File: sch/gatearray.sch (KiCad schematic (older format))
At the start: 71 parts, among them X2 CONN-7S

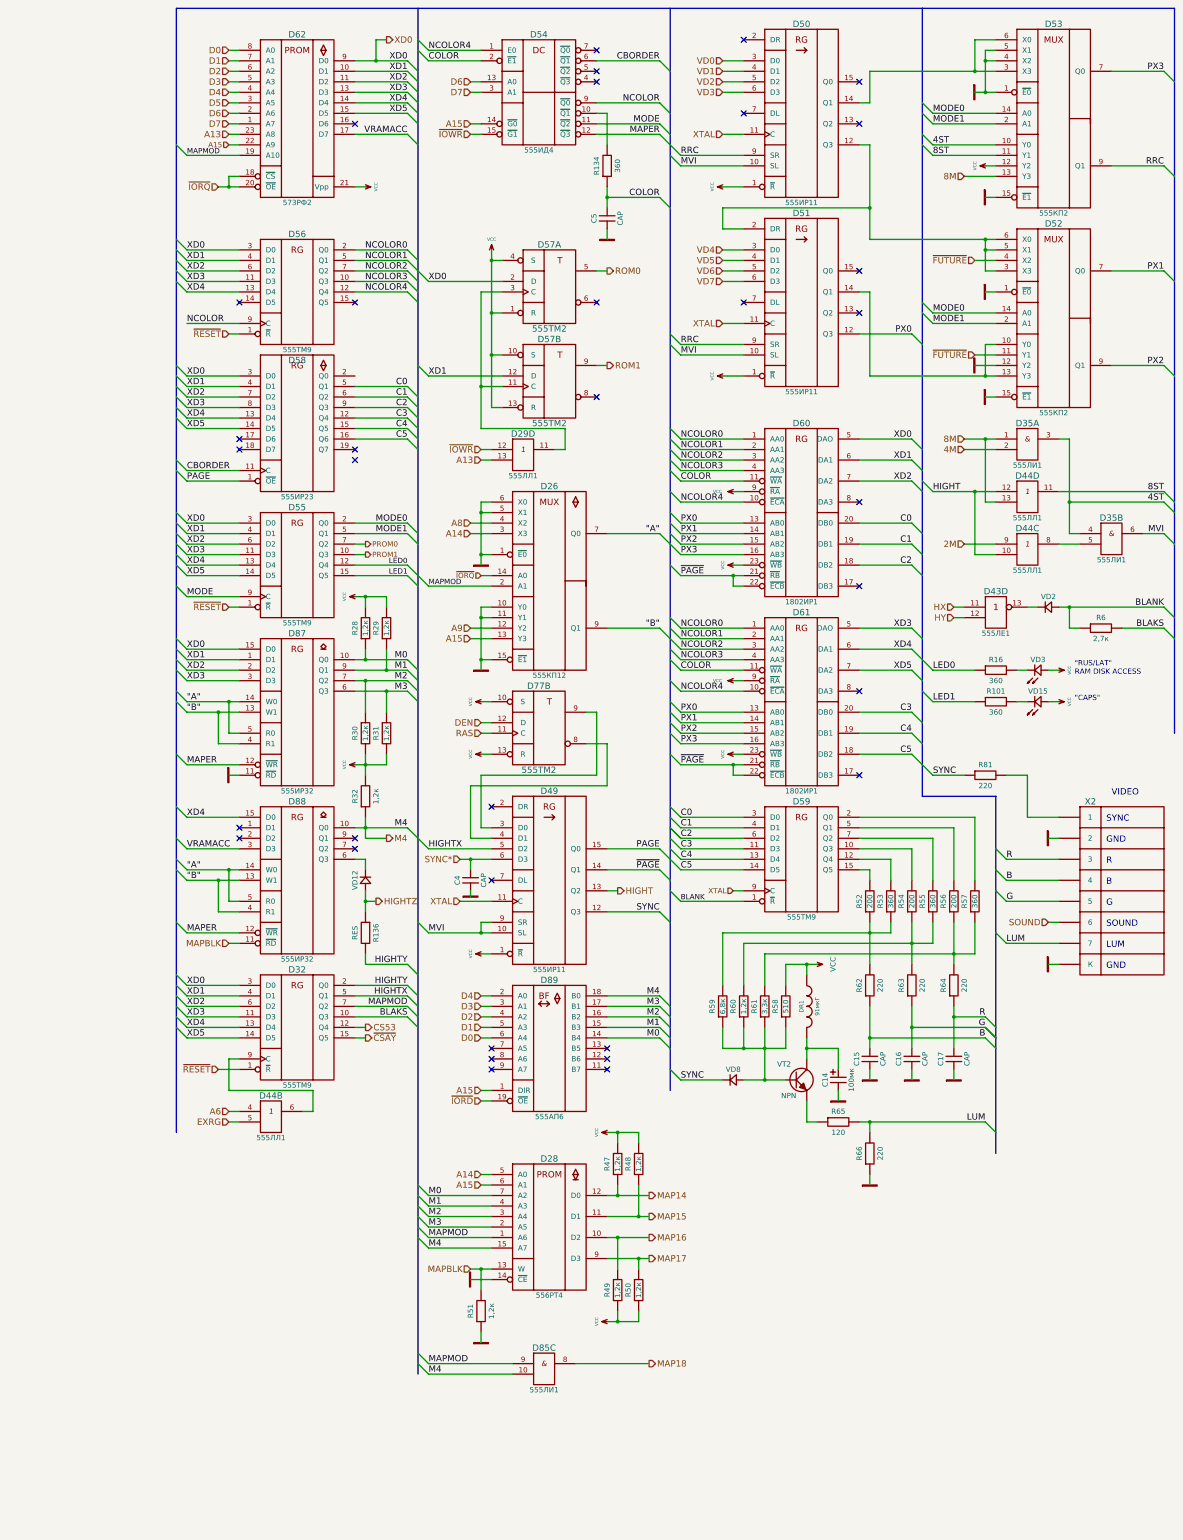
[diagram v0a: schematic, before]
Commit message: Start to move to a bit more affordable components
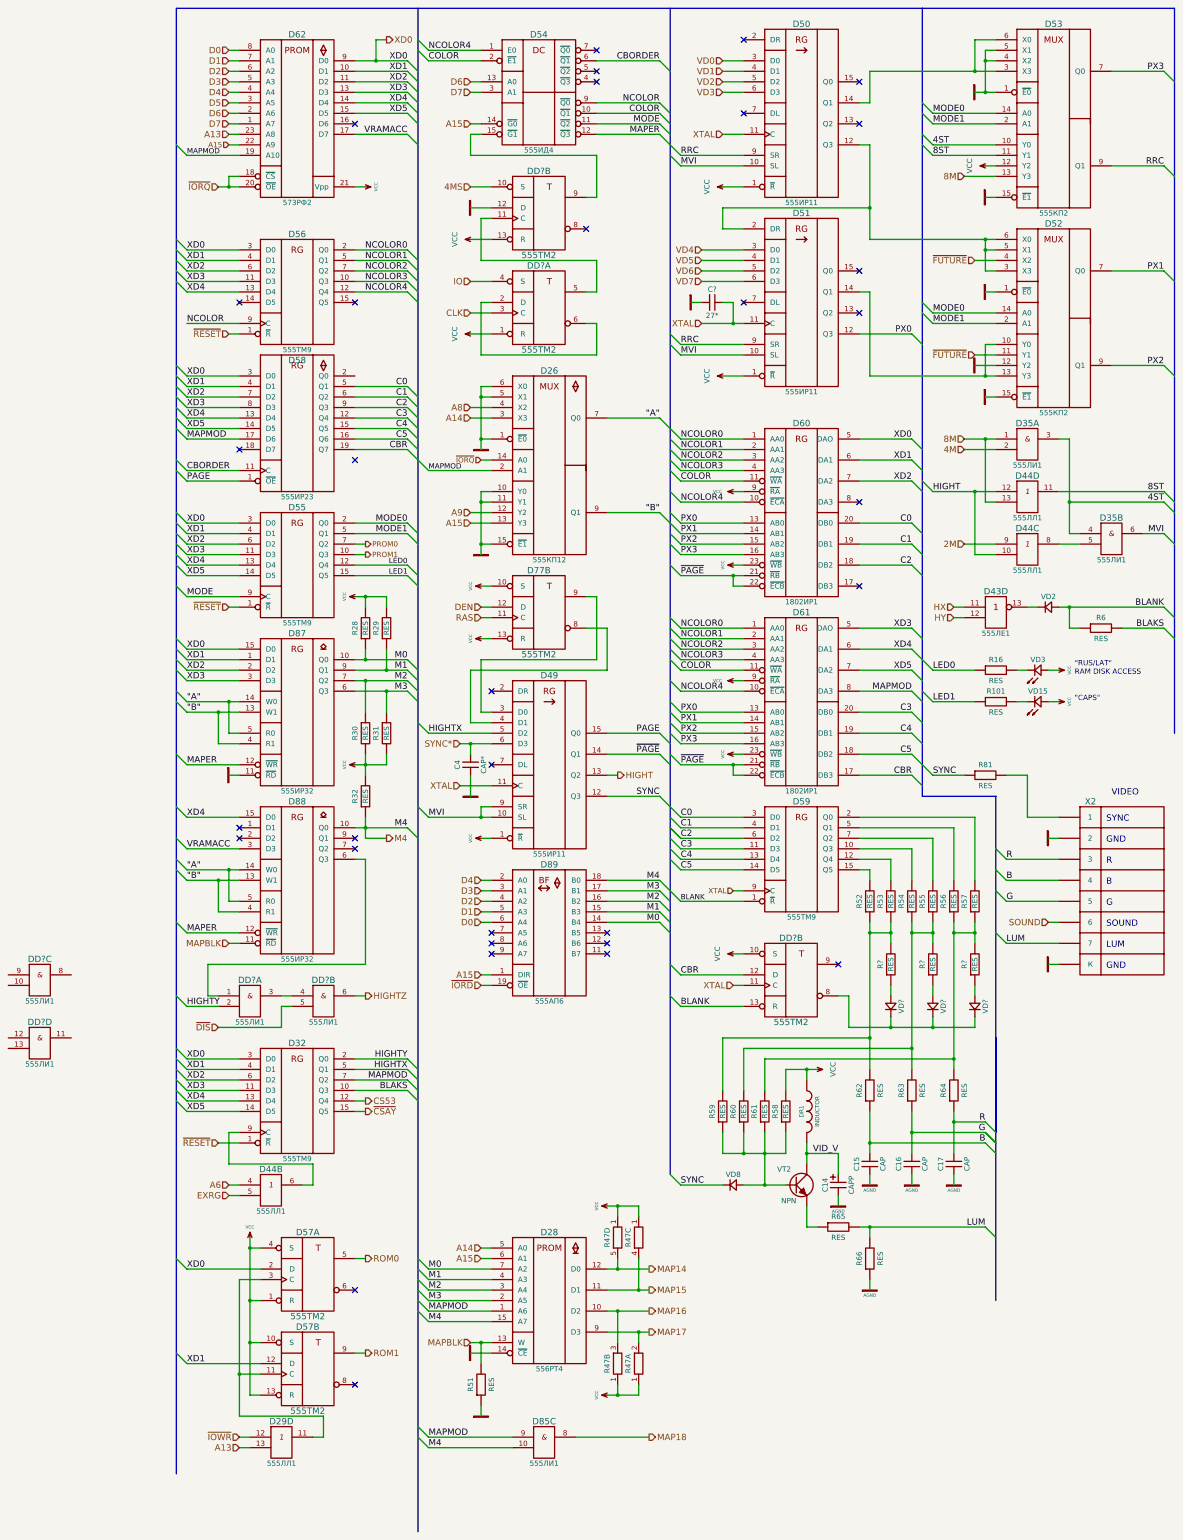
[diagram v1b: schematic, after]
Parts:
- removed C5: CAP, MyLib:C_Disc_D7.5_P2.5, symbol CAP
- removed R134: 360, MyLib:Resistor_Horizontal_RM7.5mm, symbol RES
- removed R136: RES, MyLib:Resistor_Horizontal_RM7.5mm, symbol RES
- removed R47, R48, R49, R50: 1,2к, MyLib:Resistor_Vertical_RM2.5mm, symbol RES
- removed VD12: DIODE_MY, MyLib:Diode_DO-35_SOD27_Horizontal_RM7.5, symbol DIODE_MY
- added C?: 27*, symbol CAP
- added DD? (x4): 555ЛИ1, symbol 555ЛИ1
- added DD? (x3): 555ТМ2, symbol 555ТМ2
- added R47: RES_PACK4_C, MyLib:Resistor_Array_SIP4, symbol RES_PACK4_C
- added R? (x3): RES, MyLib:Resistor_Horizontal_RM7.5mm, symbol RES
- added VD? (x3): DIODE, symbol DIODE
- C14: value 100мк -> CAPP
- C4: value CAP -> CAP*
- DR1: value 91мкГ -> INDUCTOR
- R101, R16, R53, R55, R57: value 360 -> RES
- R28, R29, R30, R31, R32, R51, R60: value 1,2к -> RES
- R52, R54, R56: value 200 -> RES
- R58: value 510 -> RES
- R59: value 6,8к -> RES
- R6: value 2,7к -> RES
- R61: value 3,3к -> RES
- R62, R63, R64, R66, R81: value 220 -> RES
- R65: value 120 -> RES
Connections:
- net BLANK: now also DD?.13 (R)
- net COLOR: now also D54.10 (~Q1)
- net GND: now also C?.1, DD?.12 (D), DD?.7 (GND), DD?.7 (GND), DD?.7 (GND), DD?.7 (GND), DD?.7 (GND), DD?.7 (GND), DD?.7 (GND)
- net HIGHTY: now also DD?.2 (in2)
- net HIGHTZ: now also DD?.6 (out)
- net MAP14: now also R47.5
- net MAP15: now also R47.4
- net MAP16: now also R47.3
- net MAP17: now also R47.2
- net MAPMOD: now also D58.17 (D6), D61.8 (DA3)
- net VCC: now also DD?.1 (R), DD?.10 (S), DD?.13 (R), DD?.14 (VCC), DD?.14 (VCC), DD?.14 (VCC), DD?.14 (VCC), DD?.14 (VCC), DD?.14 (VCC), DD?.14 (VCC), R47.1, R47.1, R47.1, R47.1
- net XTAL: now also C?.2, DD?.11 (C)
- net ~IOWR: no longer D54.15 (~G1)
- net VID_V: now reaches C14.1, DR1.2, VT2.C
- net CBR: now reaches D58.19 (Q7)
- net CBR: now also D61.17 (DB3), DD?.12 (D)
- net at D88.6 (Q3): now also DD?.1 (in1)
- net at R52.1, R53.1, R59.2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: now also R?.2
- net at R54.1, R55.1, R60.2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: now also R?.2
- net at R56.1, R57.1, R61.2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: now also R?.2
- new net: D54.15 (~G1), DD?.9
- new net: DD?.3 (out), DD?.4 (in1)
- new net: DD?.2 (D), DD?.6
- new net: DD?.11 (C), DD?.5
- new net: DD?.8, VD?.1, VD?.1, VD?.1
- new net: R?.1, VD?.2 (x3)
- new net 4MS: DD?.10 (S)
- new net CLK: DD?.3 (C)
- new net IO: DD?.4 (S)
- new net ~DIS: DD?.5 (in2)
- no-connect marks 35 -> 33
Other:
- moved on the sheet: C14, C15, C16, C17, C4, D26, D28, D29D, D32, D44B, D49, D57A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

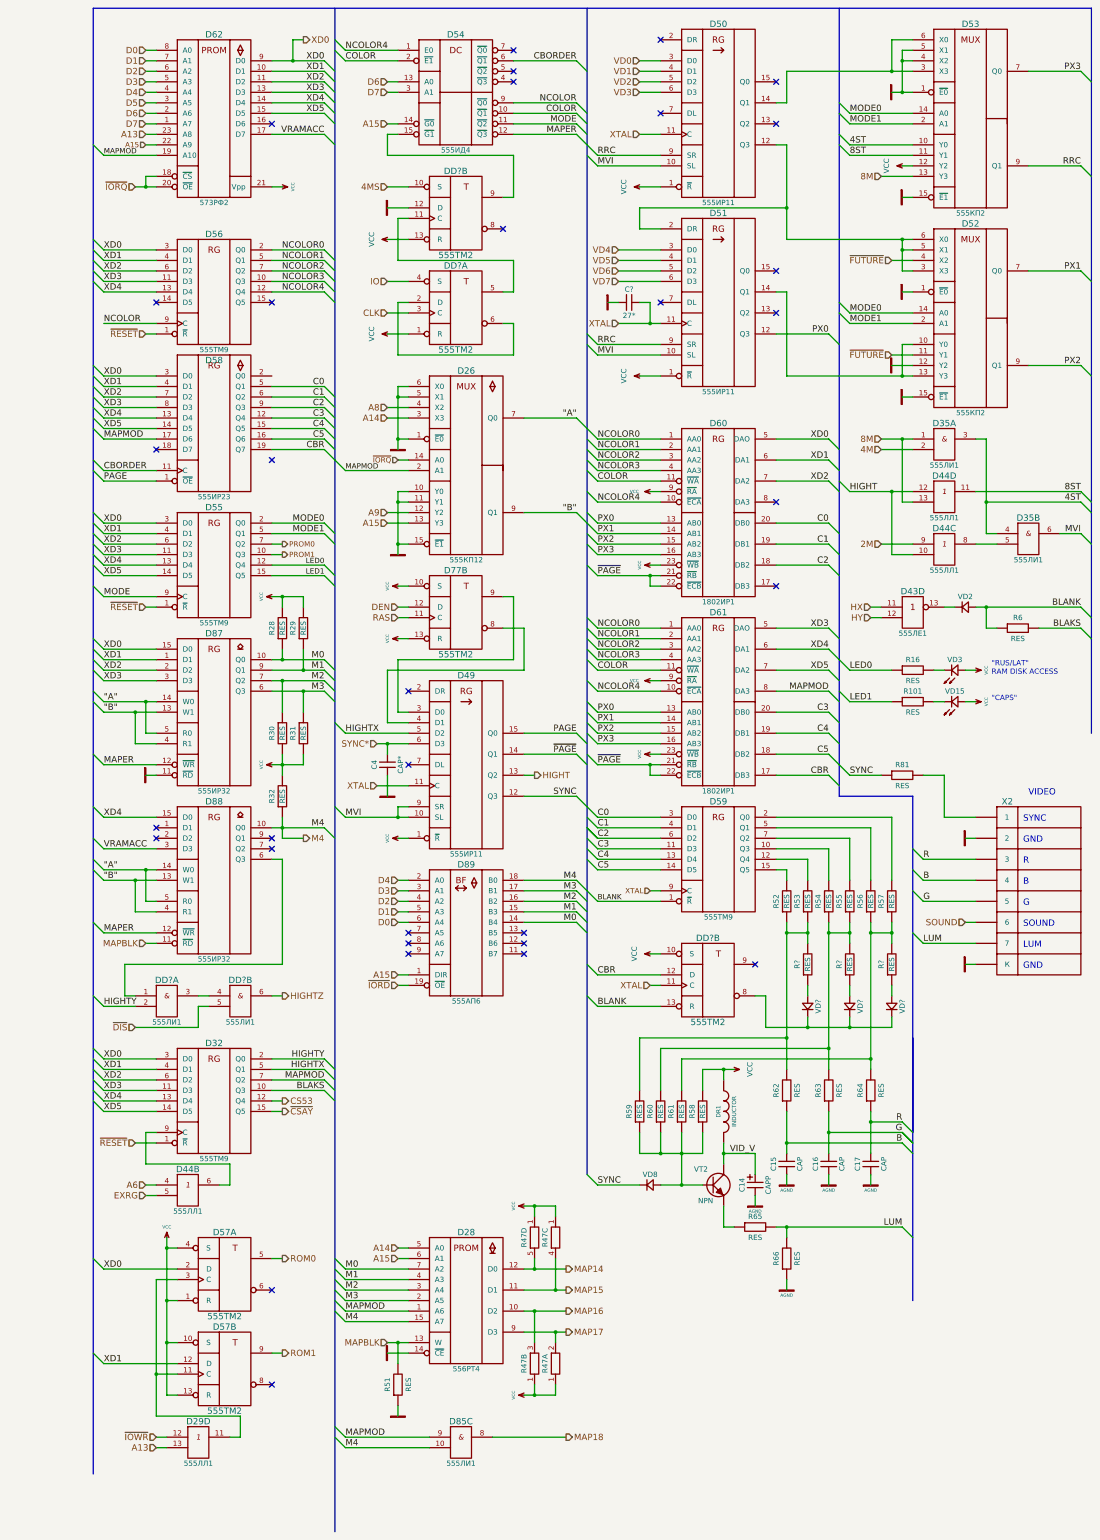
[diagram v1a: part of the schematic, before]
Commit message: Update IR22 and IR23 symbols
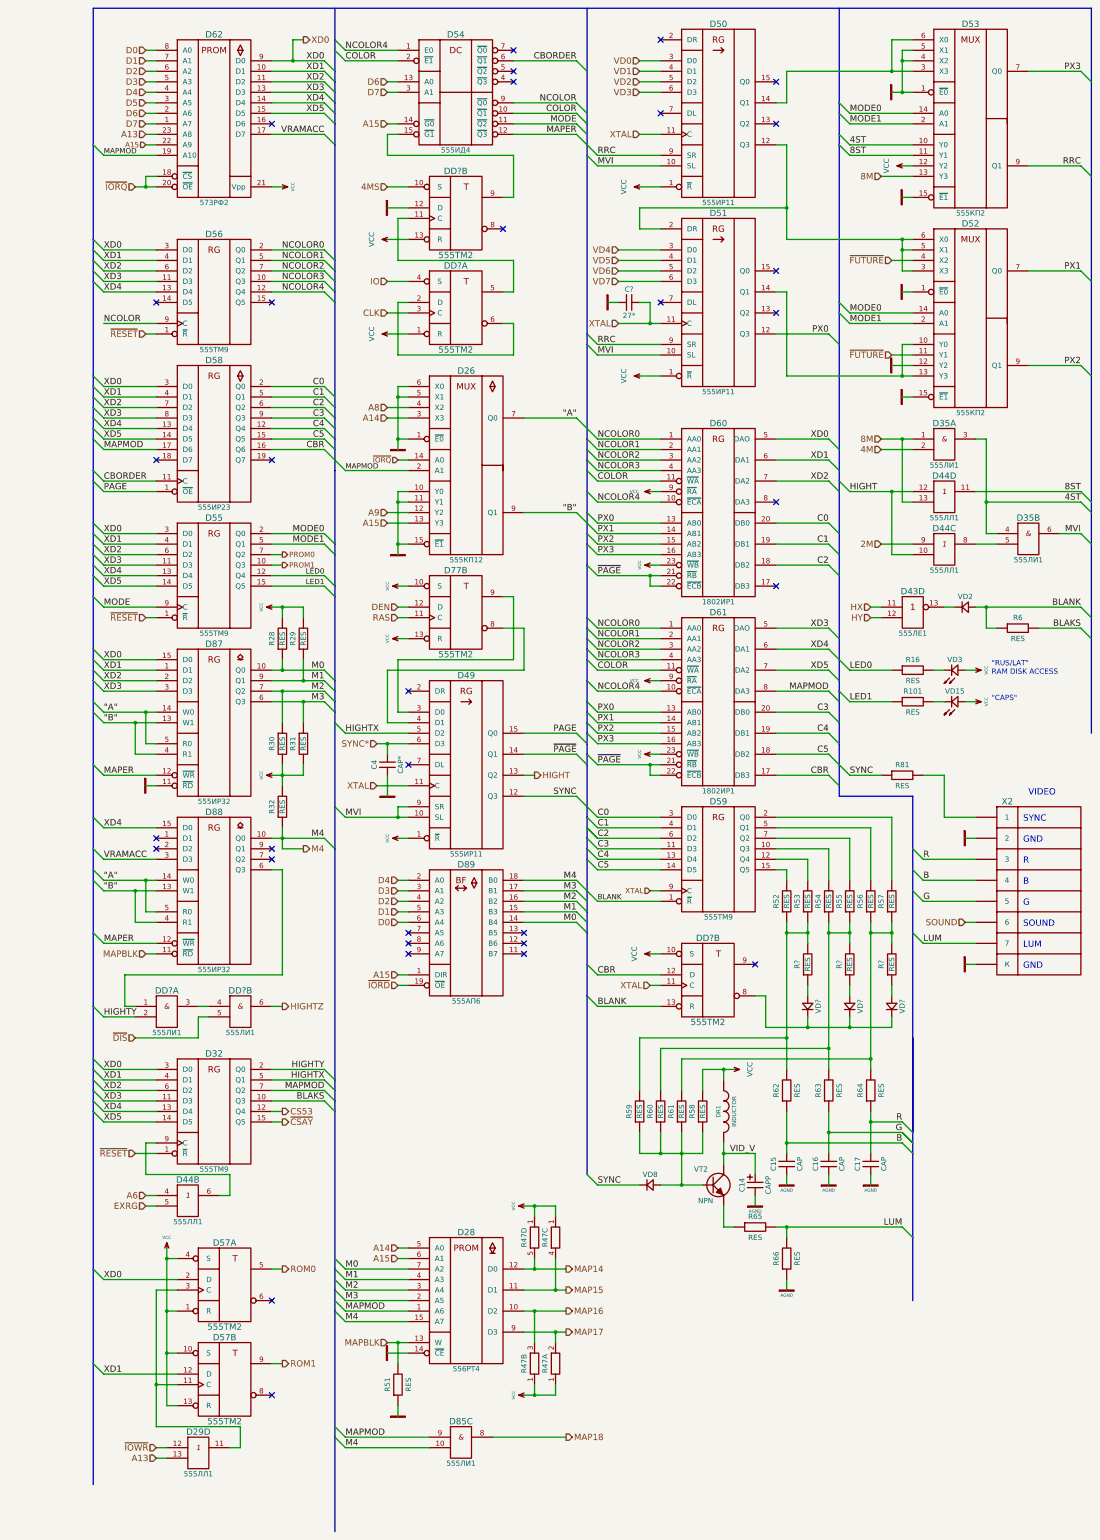
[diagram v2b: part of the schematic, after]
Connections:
- net C0: now also D58.2 (Q0); no longer D58.5 (Q1)
- net C1: now also D58.5 (Q1); no longer D58.6 (Q2)
- net C2: now also D58.6 (Q2); no longer D58.9 (Q3)
- net C3: now also D58.9 (Q3); no longer D58.12 (Q4)
- net C4: now also D58.12 (Q4); no longer D58.15 (Q5)
- net C5: now also D58.15 (Q5); no longer D58.16 (Q6)
- net CBR: now also D58.16 (Q6); no longer D58.19 (Q7)
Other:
- moved on the sheet: D29D, D32, D44B, D55, D57A, D57B, D58, D87, D88, DD?A, DD?B, R28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
